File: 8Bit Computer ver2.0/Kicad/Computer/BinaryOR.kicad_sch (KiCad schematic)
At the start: 4 parts, among them IC10 SN74HCS32DR, IC11 SN74HCS74DR, IC12 SN74ABT821ADWR, IC9 SN74LVC1G14DBVR

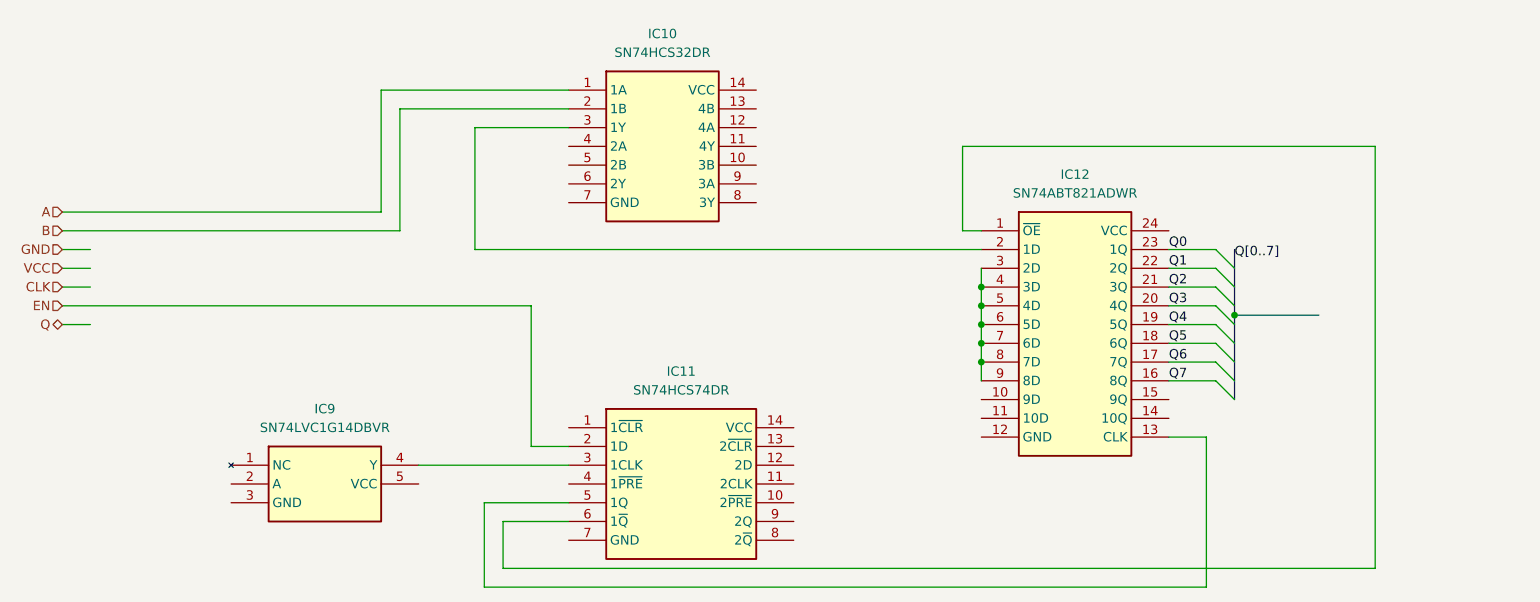
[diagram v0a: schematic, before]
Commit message: parts,Kicad
added 74HCS574 to Kicad
Kicad:
ALU->added Bitwise NOT,OR,XOR,AND
ALU->added A,B 8in OR
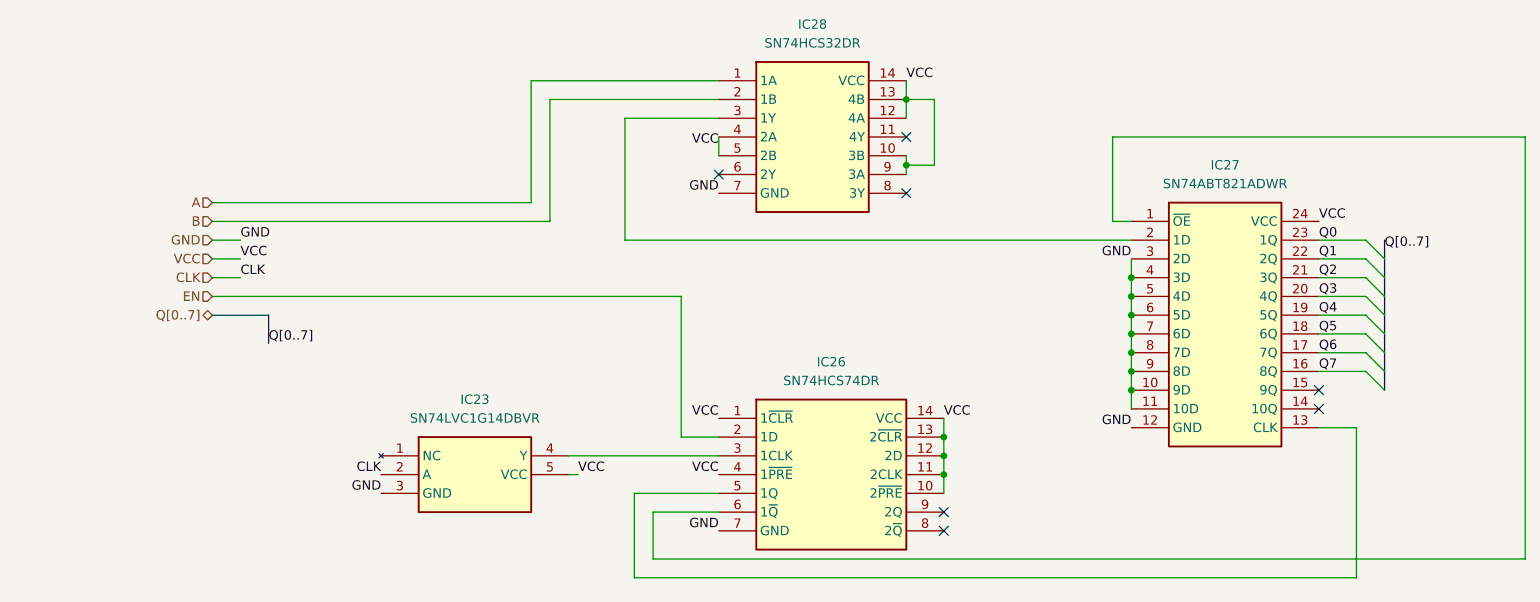
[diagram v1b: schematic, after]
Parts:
- removed IC10: SN74HCS32DR, Samacsys:SOIC127P600X175-14N, symbol Samacsys:SN74HCS32DR
- removed IC11: SN74HCS74DR, Samacsys:SOIC127P600X175-14N, symbol Samacsys:SN74HCS74DR
- removed IC12: SN74ABT821ADWR, Samacsys:SOIC127P1030X265-24N, symbol Samacsys:SN74ABT821ADWR
- removed IC9: SN74LVC1G14DBVR, Samacsys:SOT95P280X145-5N, symbol Samacsys:SN74LVC1G14DBVR
- added IC23: SN74LVC1G14DBVR, Samacsys:SOT95P280X145-5N, symbol Samacsys:SN74LVC1G14DBVR
- added IC26: SN74HCS74DR, Samacsys:SOIC127P600X175-14N, symbol Samacsys:SN74HCS74DR
- added IC27: SN74ABT821ADWR, Samacsys:SOIC127P1030X265-24N, symbol Samacsys:SN74ABT821ADWR
- added IC28: SN74HCS32DR, Samacsys:SOIC127P600X175-14N, symbol Samacsys:SN74HCS32DR
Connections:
- net A: now also IC28.1 (1A)
- net B: now also IC28.2 (1B)
- net CLK: now also IC23.2 (A)
- net EN: now also IC26.2 (1D)
- net GND: now also IC23.3 (GND), IC26.7 (GND), IC27.10 (9D), IC27.11 (10D), IC27.12 (GND), IC27.3 (2D), IC27.4 (3D), IC27.5 (4D), IC27.6 (5D), IC27.7 (6D), IC27.8 (7D), IC27.9 (8D), IC28.7 (GND)
- net Q0: now also IC27.23 (1Q)
- net Q1: now also IC27.22 (2Q)
- net Q2: now also IC27.21 (3Q)
- net Q3: now also IC27.20 (4Q)
- net Q4: now also IC27.19 (5Q)
- net Q5: now also IC27.18 (6Q)
- net Q6: now also IC27.17 (7Q)
- net Q7: now also IC27.16 (8Q)
- net VCC: now also IC23.5 (VCC), IC26.1 (1~{CLR}), IC26.10 (2~{PRE}), IC26.11 (2CLK), IC26.12 (2D), IC26.13 (2~{CLR}), IC26.14 (VCC), IC26.4 (1~{PRE}), IC27.24 (VCC), IC28.10 (3B), IC28.12 (4A), IC28.13 (4B), IC28.14 (VCC), IC28.4 (2A), IC28.5 (2B), IC28.9 (3A)
- new net: IC23.4 (Y), IC26.3 (1CLK)
- new net: IC26.5 (1Q), IC27.13 (CLK)
- new net: IC26.6 (1~{Q}), IC27.1 (~{OE})
- new net: IC27.2 (1D), IC28.3 (1Y)
- no-connect marks 0 -> 7
